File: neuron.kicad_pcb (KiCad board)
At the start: 2 copper layers, 98.5 x 59.8 mm, 67 parts, among them J1 Conn_01x03, J2 Conn_01x03, J3 Conn_01x03, J4 Conn_02x03, Q1 BSS84, Q2 2N7002, Q3 BSS84, Q4 2N7002, Q5 BSS84, Q6 2N7002, Q7 2N7002, Q8 2sk3018, U1 74HC14, U4 MCP6001-OT, U5 LM339, U6 LM339

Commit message: Update for second production run
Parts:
- R12, R13, R14, R15, R16, R17, R26: value 100k -> 56k
- R20, R21, R22, R23, R24, R25: value 100 -> 150
- R30: value 33 -> 10
- moved BT1 0.40 mm to (83.4, 66.7)
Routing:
- net /VU4: track 42.5 -> 36.9 mm
- net GND: track 35.1 -> 35.5 mm, vias 38 -> 39
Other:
- board text added: "Lu.i 10/2022 - giantaxon.org made with in Heidelberg & Bern"
- board text added: "n.einc.eu"
- board text removed: "2022 - SB, YS, JG, MAP made with in Heidelberg & Bern"

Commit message: Implement exponential synapses
Co-authored-by: Yannik Stradmann <yannik@stradmann.name>
Co-authored-by: Julian Göltz <mail@julian-goeltz.de>
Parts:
- removed the REF** at (70.8, 56.5)
- removed REF1: Probepad, Custom:Probepad
- removed U4: MCP6001-OT, Package_TO_SOT_SMD:SOT-23-5
- added C7: 100n, Capacitor_SMD:C_0402_1005Metric, F.Cu at (74.4, 75.7)
- added C8: 100n, Capacitor_SMD:C_0402_1005Metric, F.Cu at (98.6, 77.5)
- added C9: 1u ic=2, Capacitor_SMD:C_0402_1005Metric, F.Cu at (88.1, 71.4)
- added Q10: 2sk3018, Package_TO_SOT_SMD:SOT-23, F.Cu at (76.8, 74.9)
- added Q12: 2sk3018, Package_TO_SOT_SMD:SOT-23, F.Cu at (101.1, 67.1)
- added Q7: SI2301, Package_TO_SOT_SMD:SOT-23, F.Cu at (81.3, 61.6)
- added Q8: SI2302, Package_TO_SOT_SMD:SOT-23, F.Cu at (81.3, 66.0)
- added R10: 22k, Resistor_SMD:R_0402_1005Metric, F.Cu at (90.2, 60.3)
- added R11: 47k, Resistor_SMD:R_0402_1005Metric, F.Cu at (90.2, 62.9)
- added R12: 47k, Resistor_SMD:R_0402_1005Metric, F.Cu at (90.2, 65.4)
- added R13: 22k, Resistor_SMD:R_0402_1005Metric, F.Cu at (90.2, 67.9)
- added R14: 2.2k, Resistor_SMD:R_0402_1005Metric, F.Cu at (87.5, 58.4)
- added R15: 2.2k, Resistor_SMD:R_0402_1005Metric, F.Cu at (85.1, 58.4)
- added R16: 470, Resistor_SMD:R_0402_1005Metric, F.Cu at (67.1, 64.0)
- added R25: 22k, Resistor_SMD:R_0402_1005Metric, F.Cu at (77.0, 77.5)
- added R42: 470, Resistor_SMD:R_0402_1005Metric, F.Cu at (65.5, 70.1)
- added R7: 22k, Resistor_SMD:R_0402_1005Metric, F.Cu at (84.5, 69.2)
- added R8: 22k, Resistor_SMD:R_0402_1005Metric, F.Cu at (85.7, 69.2)
- added R9: 470, Resistor_SMD:R_0402_1005Metric, F.Cu at (78.2, 51.3)
- added REF**: Testpad, Custom:Testpad, F.Cu at (86.0, 55.5)
- added REF**: Testpad, Custom:Testpad, F.Cu at (105.1, 69.6)
- added RV4: 20k, Custom:Potentiometer, F.Cu at (76.2, 70.5)
- added SW1: SW_SPDT, Custom:K3-1290S-E1, F.Cu at (76.1, 49.2)
- added SW2: SW_SPDT, Custom:K3-1290S-E1, F.Cu at (60.5, 61.3)
- added SW3: SW_SPDT, Custom:K3-1290S-E1, F.Cu at (65.0, 80.3)
- BT1: value Battery_Cell -> type="R" model="Battery_Cell" lib=""
- C1: value 4.7u -> 100n; footprint Capacitor_SMD:C_0805_2012Metric -> Capacitor_SMD:C_0402_1005Metric
- C2: value 1u -> 10u ic=0.0; footprint Capacitor_SMD:C_0805_2012Metric -> Capacitor_SMD:C_0402_1005Metric
- C5: value 100n -> 22u ic=0.6
- J1, J2, J3: value Conn_01x03 -> Conn_02x01; footprint Connector_PinHeader_2.54mm:PinHeader_1x03_P2.54mm_Vertical -> Connector_PinHeader_2.54mm:PinHeader_1x02_P2.54mm_Vertical
- Q1, Q3: value BSS84 -> 2sk3018
- Q2: value 2N7002 -> 2sk3018
- Q4, Q6: value 2N7002 -> BSS84
- R22: renamed from R11; value 100k -> 22k
- R23: renamed from R19; value 100k -> 22k
- R4, R5, R6: value 100k -> 10k
- RV1, RV2, RV3: value 20k -> 5k
- RV5: renamed from RV4; value 200k -> 100k
- RV6: renamed from RV5; value 200k -> 50k
- U1: value 74HC14 -> MCP6004
- moved R2 27.9 mm to (51.4, 61.0), turned to -90 degrees
- moved R5 25.9 mm to (66.5, 57.9), turned to 0 degrees
- moved R3 25.1 mm to (55.5, 86.1), turned to 45 degrees
- moved Q3 23.6 mm to (60.7, 84.6), turned to 45 degrees
- moved C5 22.0 mm to (67.6, 67.1), turned to 180 degrees
- moved C3 21.6 mm to (67.6, 68.3), turned to 0 degrees
- moved Q2 21.6 mm to (54.6, 61.0)
- moved C4 19.4 mm to (67.6, 69.6), turned to 0 degrees
- moved U1 16.5 mm to (86.4, 63.5)
- moved Q5 15.9 mm to (66.5, 61.0), turned to -90 degrees
- moved R4 15.8 mm to (71.1, 56.6), turned to 90 degrees
- moved Q4 10.6 mm to (73.7, 55.1), turned to 0 degrees
- moved R1 9.25 mm to (78.1, 36.8), turned to 90 degrees
- moved C6 8.79 mm to (67.6, 70.9), turned to 0 degrees
- moved Q1 7.62 mm to (75.6, 43.2), turned to -90 degrees
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- renumbered Q8 to Q11, Q7 to Q9, R8 to R17, R26 to R18, R7 to R19, R18 to R20, R9 to R21, R27 to R24, R28 to R26, R29 to R27, R10 to R28, R12 to R29, R13 to R30, R14 to R31, R15 to R32, R16 to R33, R17 to R34, R20 to R35, R21 to R36, R22 to R37, R23 to R38, R24 to R39, R25 to R40, R30 to R41, U5 to U2, U6 to U3
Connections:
- C1 pad 1: /MEM -> GND
- C1 pad 2: GND -> Net-(U1B-+)
- C2 pad 1: GND -> Net-(U1B--)
- C2 pad 2: /REFR -> /VSYN
- C5 pad 1: GND -> /MEM
- C5 pad 2: VDD -> GND
- J1 pad 1: /INH1 -> GND
- J1 pad 2: GND -> Net-(J1-Pin_2)
- J2 pad 1: /INH2 -> GND
- J2 pad 2: GND -> Net-(J2-Pin_2)
- J3 pad 1: /INH3 -> GND
- J3 pad 2: GND -> Net-(J3-Pin_2)
- Q1 pad 1: Net-(Q1-Pad1) -> Net-(J1-Pin_2)
- Q1 pad 2: VDD -> GND
- Q1 pad 3: Net-(Q1-Pad3) -> Net-(Q1-D)
- Q2 pad 1: /INH1 -> Net-(J2-Pin_2)
- Q2 pad 3: Net-(Q1-Pad3) -> Net-(Q2-D)
- Q3 pad 1: Net-(Q3-Pad1) -> Net-(J3-Pin_2)
- Q3 pad 2: VDD -> GND
- Q3 pad 3: Net-(Q3-Pad3) -> Net-(Q3-D)
- Q4 pad 1: /INH2 -> Net-(Q4-G)
- Q4 pad 2: GND -> VDD
- Q4 pad 3: Net-(Q3-Pad3) -> Net-(Q4-D)
- Q5 pad 1: Net-(Q5-Pad1) -> Net-(Q5-G)
- Q5 pad 3: Net-(Q5-Pad3) -> Net-(Q5-D)
- Q6 pad 1: /INH3 -> Net-(Q6-G)
- Q6 pad 2: GND -> VDD
- Q6 pad 3: Net-(Q5-Pad3) -> Net-(Q6-D)
- R1 pad 1: /EXC1 -> Net-(J1-Pin_2)
- R2 pad 1: /INH1 -> Net-(J2-Pin_2)
- R21 pad 2: Net-(R27-Pad1) -> Net-(Q10-G)
- R24 pad 1: Net-(R27-Pad1) -> Net-(Q10-G)
- R3 pad 1: /EXC2 -> Net-(J3-Pin_2)
- R4 pad 1: /INH2 -> VDD
- R4 pad 2: GND -> Net-(Q4-G)
- R5 pad 1: /EXC3 -> VDD
- R5 pad 2: GND -> Net-(Q5-G)
- R6 pad 1: /INH3 -> VDD
- R6 pad 2: GND -> Net-(Q6-G)
- RV1 pad 1: Net-(Q1-Pad3) -> Net-(Q4-D)
- RV1 pad 2: /MEM -> Net-(R9-Pad1)
- RV1 pad 3: /MEM -> Net-(R9-Pad1)
- RV2 pad 1: Net-(Q3-Pad3) -> Net-(Q5-D)
- RV2 pad 2: /MEM -> Net-(R16-Pad1)
- RV2 pad 3: /MEM -> Net-(R16-Pad1)
- RV3 pad 1: Net-(Q5-Pad3) -> Net-(Q6-D)
- RV3 pad 2: /MEM -> Net-(R42-Pad1)
- RV3 pad 3: /MEM -> Net-(R42-Pad1)
- RV5 pad 2: Net-(RV4-Pad2) -> Net-(U1A-+)
- RV6 pad 3: Net-(RV5-Pad3) -> /VLEAK
- U1 pad 1: GND -> /VLEAK
- U1 pad 10: Net-(Q3-Pad1) -> Net-(U1C-+)
- U1 pad 11: /EXC2 -> GND
- U1 pad 12: Net-(Q5-Pad1) -> Net-(U1D-+)
- U1 pad 13: /EXC3 -> Net-(Q8-S)
- U1 pad 14: VDD -> Net-(Q8-G)
- U1 pad 2: unconnected-(U1-Pad2) -> /VLEAK
- U1 pad 3: Net-(R27-Pad1) -> Net-(U1A-+)
- U1 pad 4: /SPK -> VDD
- U1 pad 5: /RESET -> Net-(U1B-+)
- U1 pad 6: /VU7 -> Net-(U1B--)
- U1 pad 7: GND -> /VSYN
- U1 pad 8: Net-(Q1-Pad1) -> Net-(Q7-G)
- U1 pad 9: /EXC1 -> Net-(Q7-S)
- U3 pad 1: Net-(R27-Pad1) -> Net-(Q10-G)
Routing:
- net Net-(U1B--): track 0.00 -> 72.1 mm, vias 0 -> 6
- net Net-(R27-Pad1): track 33.2 -> 0.00 mm, vias 2 -> 0
- net /VU7: track 75.5 -> 42.7 mm, vias 2 -> 0
- net /EXC3: track 27.9 -> 0.00 mm, vias 1 -> 0
- net /EXC1: track 27.5 -> 0.00 mm, vias 1 -> 0
- net GND: track 35.5 -> 10.2 mm, vias 39 -> 10
- net /EXC2: track 25.1 -> 0.00 mm, vias 1 -> 0
- net /VSYN: track 0.00 -> 24.6 mm, vias 0 -> 2
- net /MEM: track 105.7 -> 81.2 mm, vias 8 -> 4
- net Net-(Q10-G): track 0.00 -> 24.0 mm, vias 0 -> 2
- net /INH2: track 22.3 -> 0.00 mm
- net Net-(Q1-Pad1): track 19.9 -> 0.00 mm, vias 2 -> 0
- net /INH1: track 19.3 -> 0.00 mm
- net /RESET: track 85.9 -> 103.8 mm
- net Net-(RV5-Pad3): track 15.6 -> 0.00 mm
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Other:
- board text added: "Lu.i 04/2023 - giantaxon.org made with by YS, SB & JG"
- board text added: "syn"
- board text removed: "Lu.i 10/2022 - giantaxon.org made with in Heidelberg & Bern"
- board text removed: "n.einc.eu"

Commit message: Clean up simulation models and testbench
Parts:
- C2: value 10u ic=0.0 -> 10u
- C5: value 22u ic=0.6 -> 22u ic=0.5
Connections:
- net Net-(J1-Pin_2) renamed /INPUT_0
- net Net-(J2-Pin_2) renamed /INPUT_1
- net Net-(J3-Pin_2) renamed /INPUT_3

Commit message: Annotate board from schematic
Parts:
- RV1, RV2, RV3: value 5k -> 22k
- RV4: value 20k -> 22k
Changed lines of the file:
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@@
     (descr "Capacitor SMD 0402 (1005 Metric), square (rectangular) end terminal, IPC_7351 nominal, (Body size source: IPC-SM-782 page 76, https://www.pcb-3d.com/wordpress/wp-content/uploads/ipc-sm-782a_amendment_1_and_2.pdf), generated with kicad-footprint-generator")
     (tags "capacitor")
-    (property "LCSC" "C2836678")
+    (property "LCSC" "C415703")
     (property "Sheetfile" "neuron.kicad_sch")
     (property "Sheetname" "")
@@
     (descr "LED SMD 0402 (1005 Metric), square (rectangular) end terminal, IPC_7351 nominal, (Body size source: http://www.tortai-tech.com/upload/download/2011102023233369053.pdf), generated with kicad-footprint-generator")
     (tags "LED")
-    (property "LCSC" "C779448")
+    (property "LCSC" "C779450")
     (property "Sheetfile" "neuron.kicad_sch")
     (property "Sheetname" "")
@@
     (descr "LED SMD 0402 (1005 Metric), square (rectangular) end terminal, IPC_7351 nominal, (Body size source: http://www.tortai-tech.com/upload/download/2011102023233369053.pdf), generated with kicad-footprint-generator")
     (tags "LED")
-    (property "LCSC" "C779448")
+    (property "LCSC" "C779450")
     (property "Sheetfile" "neuron.kicad_sch")
     (property "Sheetname" "")
@@
     (descr "LED SMD 0402 (1005 Metric), square (rectangular) end terminal, IPC_7351 nominal, (Body size source: http://www.tortai-tech.com/upload/download/2011102023233369053.pdf), generated with kicad-footprint-generator")
     (tags "LED")
-    (property "LCSC" "C779448")
+    (property "LCSC" "C779450")
     (property "Sheetfile" "neuron.kicad_sch")
     (property "Sheetname" "")
@@
   (footprint "Custom:Potentiometer" (layer "F.Cu")
     (at 79.375 54.61 180)
-    (property "LCSC" "C128557")
+    (property "LCSC" "C128552")
     (property "Sheetfile" "neuron.kicad_sch")
     (property "Sheetname" "")
@@
         (effects (font (size 1 1) (thickness 0.15)))
     )
-    (fp_text value "5k" (at 5 0 270 unlocked) (layer "F.Fab")
+    (fp_text value "22k" (at 5 0 270 unlocked) (layer "F.Fab")
         (effects (font (size 1 1) (thickness 0.15)))
     )
@@
   (footprint "Custom:Potentiometer" (layer "F.Cu")
     (at 63.5 64.008 180)
-    (property "LCSC" "C128557")
+    (property "LCSC" "C128552")
     (property "Sheetfile" "neuron.kicad_sch")
     (property "Sheetname" "")
@@
         (effects (font (size 1 1) (thickness 0.15)))
     )
-    (fp_text value "5k" (at 5 0 270 unlocked) (layer "F.Fab")
+    (fp_text value "22k" (at 5 0 270 unlocked) (layer "F.Fab")
         (effects (font (size 1 1) (thickness 0.15)))
     )
@@
     (descr "LED SMD 0402 (1005 Metric), square (rectangular) end terminal, IPC_7351 nominal, (Body size source: http://www.tortai-tech.com/upload/download/2011102023233369053.pdf), generated with kicad-footprint-generator")
     (tags "LED")
-    (property "LCSC" "C779448")
+    (property "LCSC" "C779450")
     (property "Sheetfile" "neuron.kicad_sch")
     (property "Sheetname" "")
@@
     (property "Sim.Device" "SUBCKT")
     (property "Sim.Library" "models/2N7002.mod")
-    (property "Sim.Name" "2N7002")
-    (property "Sim.Pins" "1=1 2=2 3=3")
+    (property "Sim.Name" "N7002")
+    (property "Sim.Pins" "1=20 2=30 3=10")
     (property "ki_description" "0.115A Id, 60V Vds, N-Channel MOSFET, SOT-23")
     (property "ki_keywords" "N-Channel Switching MOSFET")
@@
     (property "Sheetfile" "neuron.kicad_sch")
     (property "Sheetname" "")
-    (property "Sim.Enable" "0")
+    (property "Sim.Device" "SUBCKT")
+    (property "Sim.Library" "models/static_switch.mod")
+    (property "Sim.Name" "switch")
+    (property "Sim.Pins" "1=1 2=2 3=3")
     (property "ki_description" "Switch, single pole double throw")
     (property "ki_keywords" "switch single-pole double-throw spdt ON-ON")
@@
     (property "Sheetfile" "neuron.kicad_sch")
     (property "Sheetname" "")
-    (property "Sim.Enable" "0")
+    (property "Sim.Device" "SUBCKT")
+    (property "Sim.Library" "models/static_switch.mod")
+    (property "Sim.Name" "switch")
+    (property "Sim.Pins" "1=1 2=2 3=3")
     (property "ki_description" "Switch, single pole double throw")
     (property "ki_keywords" "switch single-pole double-throw spdt ON-ON")
@@
     (descr "LED SMD 0402 (1005 Metric), square (rectangular) end terminal, IPC_7351 nominal, (Body size source: http://www.tortai-tech.com/upload/download/2011102023233369053.pdf), generated with kicad-footprint-generator")
     (tags "LED")
-    (property "LCSC" "C779448")
+    (property "LCSC" "C779450")
     (property "Sheetfile" "neuron.kicad_sch")
     (property "Sheetname" "")
@@
   (footprint "Custom:Potentiometer" (layer "F.Cu")
     (at 67.31 74.295 180)
-    (property "LCSC" "C128557")
+    (property "LCSC" "C128552")
     (property "Sheetfile" "neuron.kicad_sch")
     (property "Sheetname" "")
@@
         (effects (font (size 1 1) (thickness 0.15)))
     )
-    (fp_text value "5k" (at 5 0 270 unlocked) (layer "F.Fab")
+    (fp_text value "22k" (at 5 0 270 unlocked) (layer "F.Fab")
         (effects (font (size 1 1) (thickness 0.15)))
     )
@@
     (descr "LED SMD 0402 (1005 Metric), square (rectangular) end terminal, IPC_7351 nominal, (Body size source: http://www.tortai-tech.com/upload/download/2011102023233369053.pdf), generated with kicad-footprint-generator")
     (tags "LED")
-    (property "LCSC" "C779448")
+    (property "LCSC" "C779450")
     (property "Sheetfile" "neuron.kicad_sch")
     (property "Sheetname" "")
@@
     (descr "LED SMD 0402 (1005 Metric), square (rectangular) end terminal, IPC_7351 nominal, (Body size source: http://www.tortai-tech.com/upload/download/2011102023233369053.pdf), generated with kicad-footprint-generator")
     (tags "LED")
-    (property "LCSC" "C779448")
+    (property "LCSC" "C779450")
     (property "Sheetfile" "neuron.kicad_sch")
     (property "Sheetname" "")
@@
     (property "Sheetfile" "neuron.kicad_sch")
     (property "Sheetname" "")
-    (property "Sim.Enable" "0")
+    (property "Sim.Device" "SUBCKT")
+    (property "Sim.Library" "models/static_switch.mod")
+    (property "Sim.Name" "switch")
+    (property "Sim.Pins" "1=1 2=2 3=3")
     (property "ki_description" "Switch, single pole double throw")
     (property "ki_keywords" "switch single-pole double-throw spdt ON-ON")
@@
   (footprint "Custom:Potentiometer" (layer "F.Cu")
     (at 76.2 70.485 180)
-    (property "LCSC" "C128550")
+    (property "LCSC" "C128552")
     (property "Sheetfile" "neuron.kicad_sch")
     (property "Sheetname" "")
@@
         (effects (font (size 1 1) (thickness 0.15)))
     )
-    (fp_text value "20k" (at 5 0 270 unlocked) (layer "F.Fab")
+    (fp_text value "22k" (at 5 0 270 unlocked) (layer "F.Fab")
         (effects (font (size 1 1) (thickness 0.15)))
     )

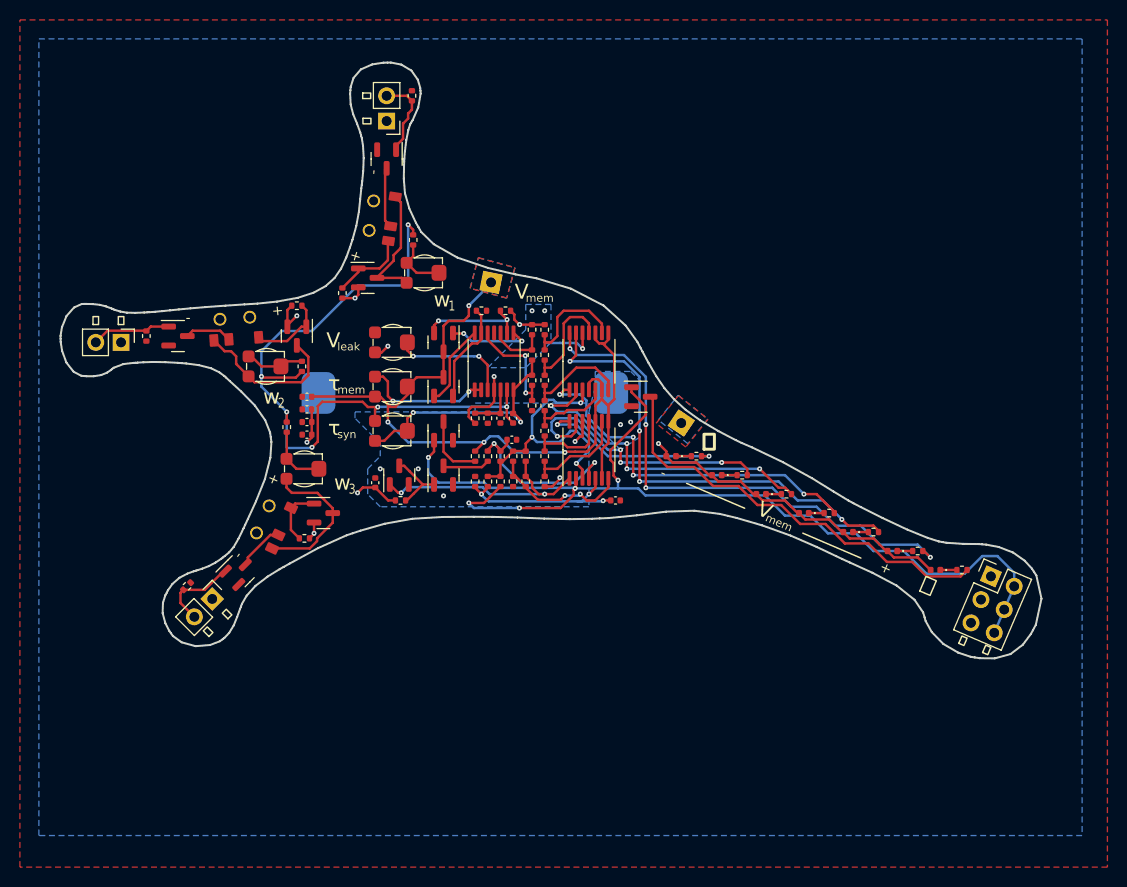
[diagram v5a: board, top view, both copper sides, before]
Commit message: Add (optional) power switch on back side
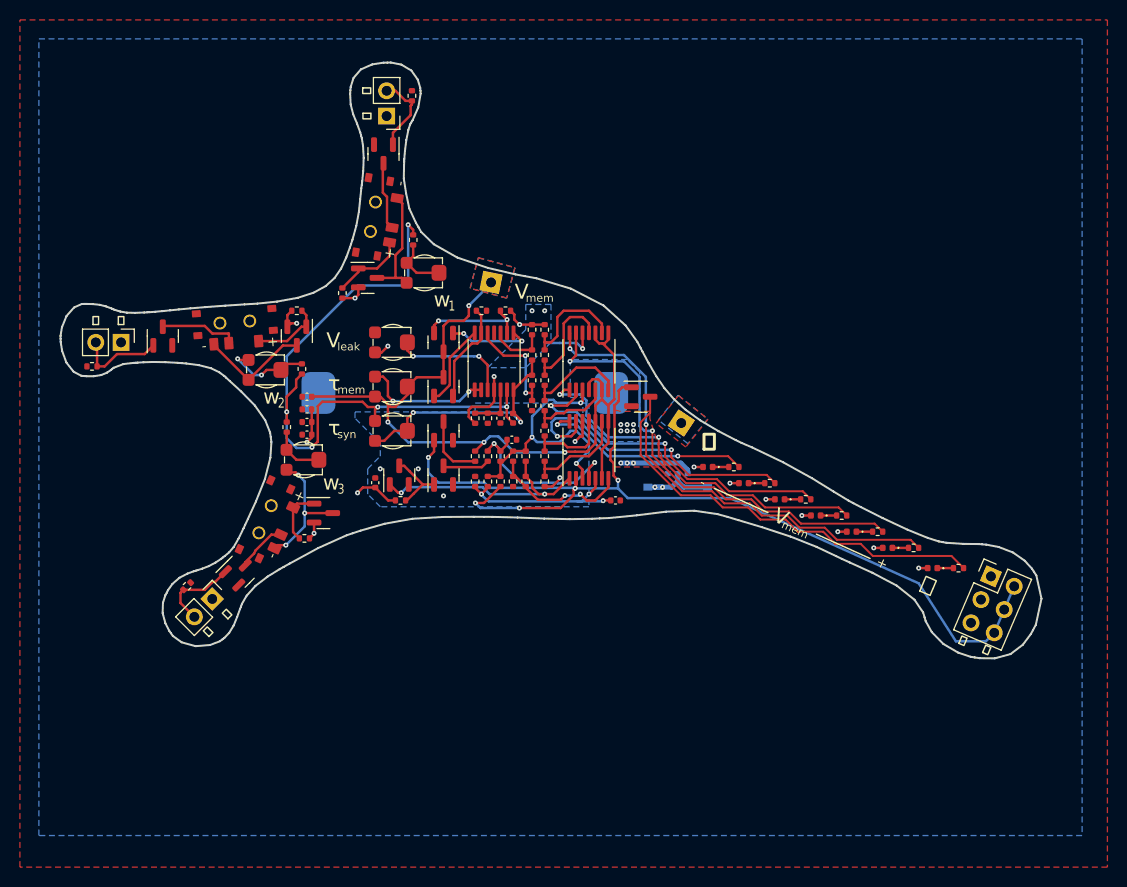
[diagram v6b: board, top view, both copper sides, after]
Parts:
- added SW4: SW_SPDT_NO_PRONGS, Custom:SSAJ120100, B.Cu at (105.8, 74.8)
- SW1, SW2, SW3: footprint Custom:K3-1290S-E1 -> Custom:K3-1296S-E1
- moved R2 6.25 mm to (46.0, 64.0), turned to 180 degrees
- moved R40 3.91 mm to (110.4, 74.1)
- moved D7 3.84 mm to (107.8, 74.1)
- moved R39 2.89 mm to (114.0, 75.7)
- moved D6 2.82 mm to (111.4, 75.7)
- moved R38 2.01 mm to (117.7, 77.4)
- moved D5 1.94 mm to (115.0, 77.4)
- moved Q2 1.52 mm to (53.1, 61.0), turned to 90 degrees
- moved SW1 1.43 mm to (74.7, 49.1), turned to -99.75 degrees
- moved SW3 1.41 mm to (63.8, 79.6), turned to -114.5 degrees
- moved R37 1.28 mm to (121.3, 79.0)
- moved SW2 1.22 mm to (60.4, 60.1)
- moved D4 1.22 mm to (118.7, 79.0)
- moved RV3 0.91 mm to (67.3, 73.4)
- moved Q1 0.60 mm to (75.2, 42.7)
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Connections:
- BT1 pad 2: GND -> GNDPWR
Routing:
- net VDD: track 89.8 -> 62.3 mm, vias 12 -> 18
- net GND: track 10.2 -> 18.3 mm
- net GNDPWR: track 0.00 -> 7.38 mm, vias 0 -> 9
- net /VU6: track 54.0 -> 49.5 mm, vias 4 -> 2
- net /RESET: track 103.8 -> 99.3 mm
- net Net-(U1B--): track 72.1 -> 67.7 mm, vias 6 -> 5
- net Net-(Q5-D): track 15.4 -> 11.3 mm
- net Net-(Q2-D): track 4.76 -> 7.88 mm
- net Net-(R16-Pad1): track 5.98 -> 8.74 mm, vias 0 -> 2
- net /VU1: track 18.7 -> 21.4 mm
- net /VU2: track 28.0 -> 30.5 mm, vias 4 -> 2
- net Net-(Q6-D): track 15.2 -> 13.5 mm, vias 0 -> 3
- net /VU5: track 47.4 -> 45.9 mm, vias 4 -> 2
- net /VU3: track 32.9 -> 34.3 mm, vias 4 -> 2
- net /INPUT_1: track 8.00 -> 8.99 mm
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- added copper zone on B.Cu, net GNDPWR
- added copper zone on F.Cu, net GNDPWR
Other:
- outline, holes or cut-outs redrawn
- board text added: "Lu.i 09/2023 - giantaxon.org made with by YS, SB & JG"
- board text added: "Uni HD, co-funded by the EU"
- board text added: "n.brainscales.eu"
- board text removed: "Lu.i 04/2023 - giantaxon.org made with by YS, SB & JG"
